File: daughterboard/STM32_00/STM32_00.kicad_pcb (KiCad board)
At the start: 4 copper layers, 67 x 50 mm, 2 parts, among them J1 m2_keyA_67pin_daughterboard

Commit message: finished layout of STM32 daughterboard
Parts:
- added C1: 100n, Capacitor_SMD:C_0603_1608Metric_Pad1.05x0.95mm_HandSolder, B.Cu at (134.1, 113.3)
- added C10: 100n, Capacitor_SMD:C_0603_1608Metric_Pad1.05x0.95mm_HandSolder, F.Cu at (136.6, 111.0)
- added C11: 4.7u, Capacitor_SMD:C_0603_1608Metric_Pad1.05x0.95mm_HandSolder, F.Cu at (139.1, 114.6)
- added C12: 100n, Capacitor_SMD:C_0603_1608Metric_Pad1.05x0.95mm_HandSolder, F.Cu at (158.9, 113.3)
- added C13: 10u, Capacitor_SMD:C_0603_1608Metric_Pad1.05x0.95mm_HandSolder, F.Cu at (171.4, 100.6)
- added C14: 100n, Capacitor_SMD:C_0603_1608Metric_Pad1.05x0.95mm_HandSolder, F.Cu at (159.2, 100.6)
- added C15: 100n, Capacitor_SMD:C_0603_1608Metric_Pad1.05x0.95mm_HandSolder, F.Cu at (158.9, 110.2)
- added C16: 100n, Capacitor_SMD:C_0603_1608Metric_Pad1.05x0.95mm_HandSolder, F.Cu at (166.3, 113.0)
- added C18: 100n, Capacitor_SMD:C_0603_1608Metric_Pad1.05x0.95mm_HandSolder, B.Cu at (155.4, 110.2)
- added C19: 4.7u, Capacitor_SMD:C_0603_1608Metric_Pad1.05x0.95mm_HandSolder, B.Cu at (171.4, 98.8)
- added C2: 4.7u, Capacitor_SMD:C_0603_1608Metric_Pad1.05x0.95mm_HandSolder, B.Cu at (124.1, 105.9)
- added C20: 100n, Capacitor_SMD:C_0603_1608Metric_Pad1.05x0.95mm_HandSolder, B.Cu at (158.9, 110.2)
- added C21: 100n, Capacitor_SMD:C_0603_1608Metric_Pad1.05x0.95mm_HandSolder, B.Cu at (171.4, 110.0)
- added C22: 100n, Capacitor_SMD:C_0603_1608Metric_Pad1.05x0.95mm_HandSolder, B.Cu at (171.4, 100.6)
- added C23: 100n, Capacitor_SMD:C_0603_1608Metric_Pad1.05x0.95mm_HandSolder, B.Cu at (157.7, 105.7)
- added C3: 4.7u, Capacitor_SMD:C_0603_1608Metric_Pad1.05x0.95mm_HandSolder, B.Cu at (135.3, 99.8)
- added C4: 100n, Capacitor_SMD:C_0603_1608Metric_Pad1.05x0.95mm_HandSolder, B.Cu at (124.1, 103.6)
- added C5: 100n, Capacitor_SMD:C_0603_1608Metric_Pad1.05x0.95mm_HandSolder, B.Cu at (130.0, 113.3)
- added C6: 100n, Capacitor_SMD:C_0603_1608Metric_Pad1.05x0.95mm_HandSolder, B.Cu at (136.6, 111.0)
- added C7: 100n, Capacitor_SMD:C_0603_1608Metric_Pad1.05x0.95mm_HandSolder, B.Cu at (135.3, 101.9)
- added C9: 100n, Capacitor_SMD:C_0603_1608Metric_Pad1.05x0.95mm_HandSolder, F.Cu at (129.0, 98.5)
- added JP1: NRST1, Jumper:SolderJumper-2_P1.3mm_Open_TrianglePad1.0x1.5mm, B.Cu at (132.0, 113.3)
- added JP2: NJRST1, Jumper:SolderJumper-2_P1.3mm_Open_TrianglePad1.0x1.5mm, B.Cu at (142.1, 105.7)
- added JP3: NRST0, Jumper:SolderJumper-2_P1.3mm_Open_TrianglePad1.0x1.5mm, F.Cu at (129.0, 102.0)
- added JP4: NRST2, Jumper:SolderJumper-2_P1.3mm_Open_TrianglePad1.0x1.5mm, F.Cu at (162.2, 113.6)
- added JP5: NJRST2, Jumper:SolderJumper-2_P1.3mm_Open_TrianglePad1.0x1.5mm, F.Cu at (163.3, 97.8)
- added JP6: NRST3, Jumper:SolderJumper-2_P1.3mm_Open_TrianglePad1.0x1.5mm, B.Cu at (157.7, 107.7)
- added JP7: NJRST3, Jumper:SolderJumper-2_P1.3mm_Open_TrianglePad1.0x1.5mm, B.Cu at (171.4, 112.3)
- added R1: 100k, Resistor_SMD:R_0603_1608Metric_Pad1.05x0.95mm_HandSolder, B.Cu at (138.1, 111.0)
- added R2: 100k, Resistor_SMD:R_0603_1608Metric_Pad1.05x0.95mm_HandSolder, F.Cu at (135.0, 121.0)
- added R3: 100k, Resistor_SMD:R_0603_1608Metric_Pad1.05x0.95mm_HandSolder, F.Cu at (135.0, 124.0)
- added R4: 100k, Resistor_SMD:R_0603_1608Metric_Pad1.05x0.95mm_HandSolder, F.Cu at (157.7, 107.2)
- added R5: 100k, Resistor_SMD:R_0603_1608Metric_Pad1.05x0.95mm_HandSolder, B.Cu at (164.5, 113.0)
- added TP1: JTMS-SWDIO, TestPoint:TestPoint_Pad_1.0x1.0mm, B.Cu at (137.4, 114.3)
- added TP12: SWDIO, TestPoint:TestPoint_Pad_1.0x1.0mm, F.Cu at (133.3, 116.0)
- added TP13: SWCLK, TestPoint:TestPoint_Pad_1.0x1.0mm, F.Cu at (131.0, 116.0)
- added TP16: USART1_TX, TestPoint:TestPoint_Pad_1.0x1.0mm, F.Cu at (128.7, 116.0)
- added TP17: USART1_RX, TestPoint:TestPoint_Pad_1.0x1.0mm, F.Cu at (135.5, 116.0)
- added TP2: JTCK-SWCLK, TestPoint:TestPoint_Pad_1.0x1.0mm, B.Cu at (144.7, 110.5)
- added TP22: JTMS-SWDIO, TestPoint:TestPoint_Pad_1.0x1.0mm, F.Cu at (153.4, 108.5)
- added TP23: JTCK-SWCLK, TestPoint:TestPoint_Pad_1.0x1.0mm, F.Cu at (148.8, 105.2)
- added TP24: JTDO-SWO, TestPoint:TestPoint_Pad_1.0x1.0mm, F.Cu at (153.4, 105.2)
- added TP25: JTDI, TestPoint:TestPoint_Pad_1.0x1.0mm, F.Cu at (151.1, 105.2)
- added TP27: USART1_TX, TestPoint:TestPoint_Pad_1.0x1.0mm, F.Cu at (159.4, 117.3)
- added TP28: USART1_RX, TestPoint:TestPoint_Pad_1.0x1.0mm, F.Cu at (156.7, 117.3)
- added TP3: JTDO-SWO, TestPoint:TestPoint_Pad_1.0x1.0mm, B.Cu at (140.1, 110.5)
- added TP33: JTMS-SWDIO, TestPoint:TestPoint_Pad_1.0x1.0mm, B.Cu at (170.9, 116.8)
- added TP34: JTCK-SWCLK, TestPoint:TestPoint_Pad_1.0x1.0mm, B.Cu at (168.6, 116.8)
- added TP35: JTDO-SWO, TestPoint:TestPoint_Pad_1.0x1.0mm, B.Cu at (164.0, 116.8)
- added TP36: JTDI, TestPoint:TestPoint_Pad_1.0x1.0mm, B.Cu at (166.3, 116.8)
- added TP38: USART1_TX, TestPoint:TestPoint_Pad_1.0x1.0mm, B.Cu at (154.9, 114.6)
- added TP39: USART1_RX, TestPoint:TestPoint_Pad_1.0x1.0mm, B.Cu at (154.9, 112.3)
- added TP4: JTDI, TestPoint:TestPoint_Pad_1.0x1.0mm, B.Cu at (142.4, 110.5)
- added TP6: USART1_TX, TestPoint:TestPoint_Pad_1.0x1.0mm, B.Cu at (124.1, 114.6)
- added TP7: USART1_RX, TestPoint:TestPoint_Pad_1.0x1.0mm, B.Cu at (126.4, 114.6)
- added U0: STM32G031F4P6, hive_daughterboard:SOP65P640X120-20N, F.Cu at (131.0, 109.0)
- added U1: STM32F401CCUx, Package_DFN_QFN:QFN-48-1EP_7x7mm_P0.5mm_EP5.6x5.6mm, B.Cu at (130.7, 107.1)
- added U2: STM32L151C8TxA, Package_QFP:LQFP-48_7x7mm_P0.5mm, F.Cu at (165.3, 105.4)
- added U3: STM32F103C8Tx, Package_QFP:LQFP-48_7x7mm_P0.5mm, B.Cu at (165.3, 105.4)
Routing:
- net GND: track 28.1 -> 195.3 mm, vias 6 -> 39
- net +3V3: track 11.6 -> 53.6 mm, vias 2 -> 16
- net /Target 1/UART_RxD1: track 0.00 -> 41.6 mm, vias 0 -> 2
- net /Target 3/TMS|SWDIO_3: track 0.00 -> 40.9 mm, vias 0 -> 4
- net /Target 3/UART_RxD3: track 0.00 -> 40.9 mm, vias 0 -> 4
- net /Target 3/UART_TxD3: track 0.00 -> 40.6 mm, vias 0 -> 4
- net /Target 0/RST_0: track 0.00 -> 39.7 mm, vias 0 -> 2
- net /Target 2/TCK|SWDCLK_2: track 0.00 -> 38.8 mm, vias 0 -> 2
- net /Target 3/GPIO3.3: track 0.00 -> 38.3 mm
- net /Target 2/TMS|SWDIO_2: track 0.00 -> 38.1 mm, vias 0 -> 2
- net /Target 2/TDI|NC_2: track 0.00 -> 37.5 mm
- net /Target 1/UART_TxD1: track 0.00 -> 37.2 mm, vias 0 -> 2
- net /Target 2/TDO|SWO_2: track 0.00 -> 35.6 mm
- net /Target 3/GPIO3.2: track 0.00 -> 35.5 mm
- net /Target 3/GPIO3.1: track 0.00 -> 35.3 mm
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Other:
- board text added: "Hive Daughterboard STM32_00 Thierry Kühni"
- board text removed: "Hive Daughterboard PROJECT FOLDER NAME YOUR NAME"

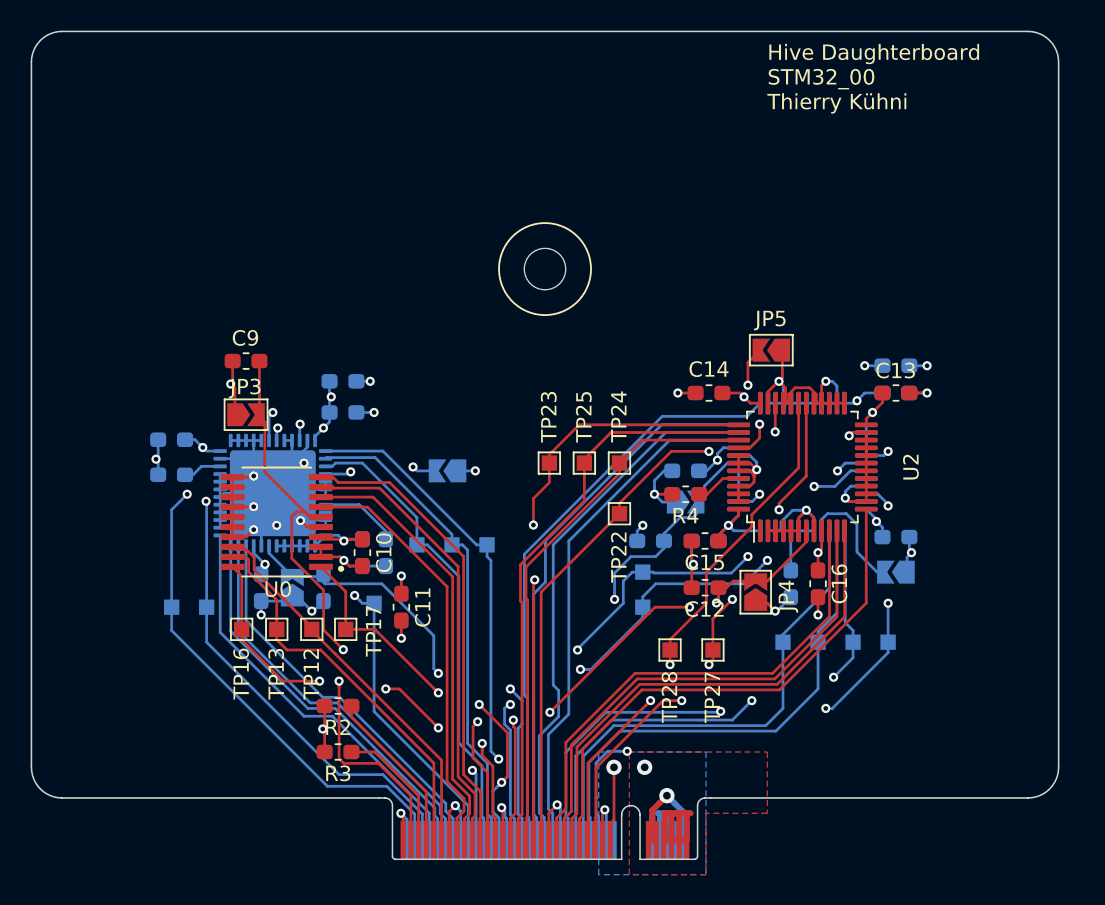
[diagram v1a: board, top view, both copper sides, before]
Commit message: length matching daughterboards
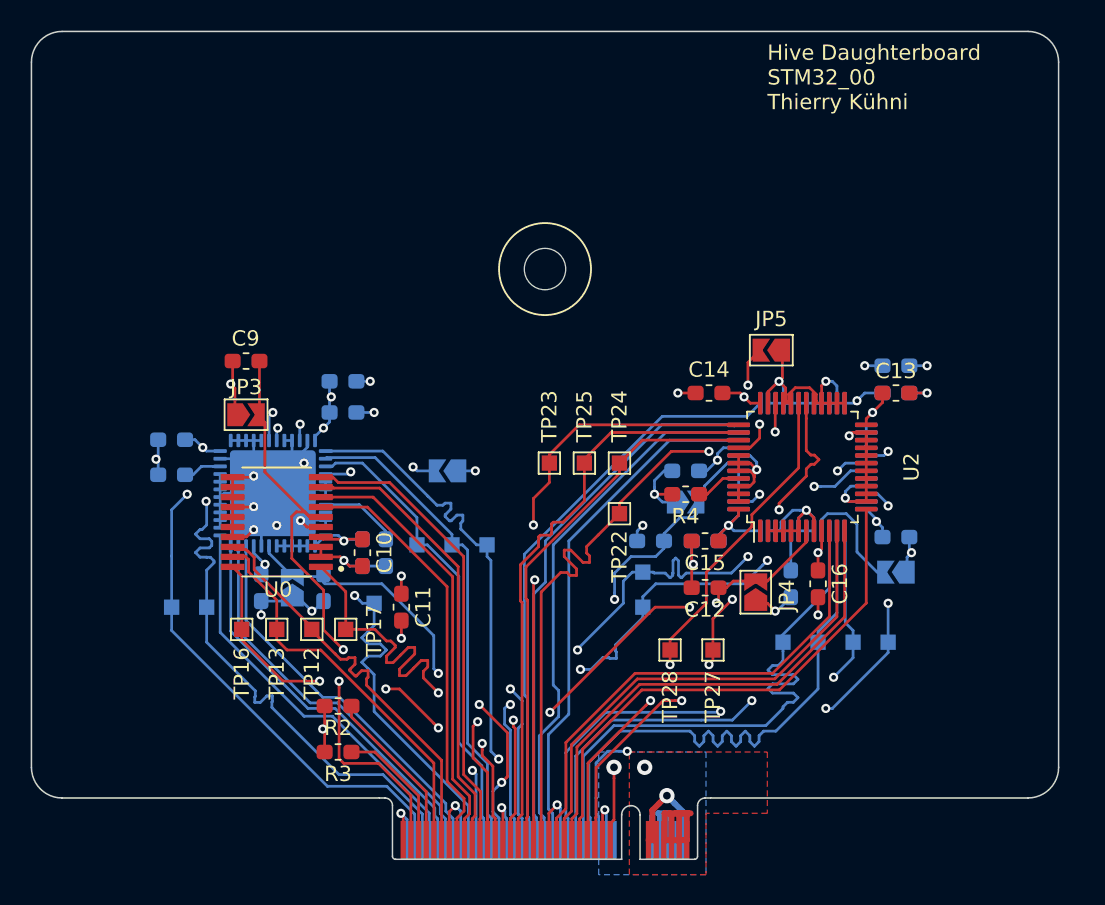
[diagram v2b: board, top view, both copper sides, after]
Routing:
- net /Target 0/UART_TxD0: track 24.1 -> 30.7 mm
- net /Target 3/TDO|SWO_3: track 32.8 -> 38.9 mm
- net /Target 3/TDI|NC_3: track 32.9 -> 38.0 mm
- net /Target 1/UART_TxD1: track 37.2 -> 41.6 mm
- net /Target 2/TMS|SWDIO_2: track 38.1 -> 41.9 mm
- net /Target 1/TMS|SWDIO_1: track 33.2 -> 36.2 mm
- net /Target 3/TCK|SWDCLK_3: track 34.7 -> 37.7 mm
- net /Target 3/UART_TxD3: track 40.6 -> 43.0 mm
- net /Target 1/TCK|SWDCLK_1: track 34.0 -> 36.2 mm
- net /Target 2/TCK|SWDCLK_2: track 38.8 -> 40.9 mm
- net /Target 0/TMS|SWDIO_0: track 25.2 -> 27.3 mm
- net /Target 2/UART_RxD2: track 34.9 -> 35.9 mm
- net /Target 2/TDI|NC_2: track 37.5 -> 38.3 mm
- net /Target 3/UART_RxD3: track 40.9 -> 41.5 mm
